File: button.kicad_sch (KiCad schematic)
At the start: 4 parts

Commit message: started to work on power part
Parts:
- SW1: renamed from SW?; footprint (none) -> Button_Switch_SMD:SW_Push_1P1T_NO_6x6mm_H9.5mm
- gave numbers to parts that had none: 3
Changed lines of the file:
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@@
   (symbol (lib_id "power:GND") (at 108.585 89.535 0) (unit 1)
     (in_bom yes) (on_board yes) (fields_autoplaced)
-    (property "Reference" "#PWR?" (id 0) (at 108.585 95.885 0)
+    (property "Reference" "#PWR030" (id 0) (at 108.585 95.885 0)
       (effects (font (size 1.27 1.27)) hide)
     )
@@
   (symbol (lib_id "Switch:SW_Push") (at 108.585 82.55 270) (unit 1)
     (in_bom yes) (on_board yes) (fields_autoplaced)
-    (property "Reference" "SW?" (id 0) (at 113.03 81.2799 90)
+    (property "Reference" "SW1" (id 0) (at 113.03 81.2799 90)
       (effects (font (size 1.27 1.27)) (justify left))
     )
@@
       (effects (font (size 1.27 1.27)) (justify left))
     )
-    (property "Footprint" "" (id 2) (at 113.665 82.55 0)
+    (property "Footprint" "Button_Switch_SMD:SW_Push_1P1T_NO_6x6mm_H9.5mm" (id 2) (at 113.665 82.55 0)
       (effects (font (size 1.27 1.27)) hide)
     )
@@
   (symbol (lib_id "eurorack:R-10k-1206") (at 108.585 71.755 0) (unit 1)
     (in_bom yes) (on_board yes) (fields_autoplaced)
-    (property "Reference" "R?" (id 0) (at 110.49 70.4849 0)
+    (property "Reference" "R28" (id 0) (at 110.49 70.4849 0)
       (effects (font (size 1.27 1.27)) (justify left))
     )
@@
   (symbol (lib_id "eurorack:C-100nF-0805") (at 96.52 83.185 0) (unit 1)
     (in_bom yes) (on_board yes)
-    (property "Reference" "C?" (id 0) (at 97.79 85.725 0)
+    (property "Reference" "C9" (id 0) (at 97.79 85.725 0)
       (effects (font (size 1.27 1.27)) (justify left))
     )
@@
   (symbol (lib_id "power:+3V3") (at 108.585 66.04 0) (unit 1)
     (in_bom yes) (on_board yes) (fields_autoplaced)
-    (property "Reference" "#PWR?" (id 0) (at 108.585 69.85 0)
+    (property "Reference" "#PWR029" (id 0) (at 108.585 69.85 0)
       (effects (font (size 1.27 1.27)) hide)
     )
@@
   (symbol (lib_id "eurorack:R-100-1206") (at 102.87 77.47 270) (unit 1)
     (in_bom yes) (on_board yes)
-    (property "Reference" "R?" (id 0) (at 101.6 80.01 90))
+    (property "Reference" "R27" (id 0) (at 101.6 80.01 90))
     (property "Value" "R-100-1206" (id 1) (at 99.06 74.93 90))
     (property "Footprint" "Resistor_SMD:R_1206_3216Metric_Pad1.30x1.75mm_HandSolder" (id 2) (at 102.87 75.692 90)

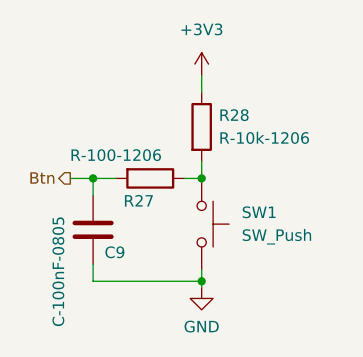
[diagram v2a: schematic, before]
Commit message: refactoring with global labels
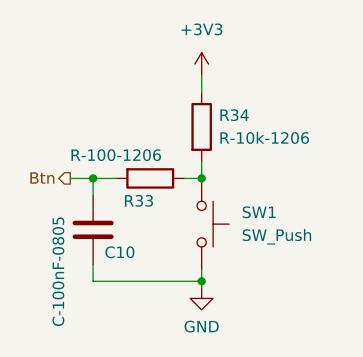
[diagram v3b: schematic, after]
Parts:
- renumbered C9 to C10, R27 to R33, R28 to R34
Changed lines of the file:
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@@
   (symbol (lib_id "power:GND") (at 108.585 89.535 0) (unit 1)
     (in_bom yes) (on_board yes) (fields_autoplaced)
-    (property "Reference" "#PWR030" (id 0) (at 108.585 95.885 0)
+    (property "Reference" "#PWR036" (id 0) (at 108.585 95.885 0)
       (effects (font (size 1.27 1.27)) hide)
     )
@@
   (symbol (lib_id "eurorack:R-10k-1206") (at 108.585 71.755 0) (unit 1)
     (in_bom yes) (on_board yes) (fields_autoplaced)
-    (property "Reference" "R28" (id 0) (at 110.49 70.4849 0)
+    (property "Reference" "R34" (id 0) (at 110.49 70.4849 0)
       (effects (font (size 1.27 1.27)) (justify left))
     )
@@
   (symbol (lib_id "eurorack:C-100nF-0805") (at 96.52 83.185 0) (unit 1)
     (in_bom yes) (on_board yes)
-    (property "Reference" "C9" (id 0) (at 97.79 85.725 0)
+    (property "Reference" "C10" (id 0) (at 97.79 85.725 0)
       (effects (font (size 1.27 1.27)) (justify left))
     )
@@
   (symbol (lib_id "power:+3V3") (at 108.585 66.04 0) (unit 1)
     (in_bom yes) (on_board yes) (fields_autoplaced)
-    (property "Reference" "#PWR029" (id 0) (at 108.585 69.85 0)
+    (property "Reference" "#PWR035" (id 0) (at 108.585 69.85 0)
       (effects (font (size 1.27 1.27)) hide)
     )
@@
   (symbol (lib_id "eurorack:R-100-1206") (at 102.87 77.47 270) (unit 1)
     (in_bom yes) (on_board yes)
-    (property "Reference" "R27" (id 0) (at 101.6 80.01 90))
+    (property "Reference" "R33" (id 0) (at 101.6 80.01 90))
     (property "Value" "R-100-1206" (id 1) (at 99.06 74.93 90))
     (property "Footprint" "Resistor_SMD:R_1206_3216Metric_Pad1.30x1.75mm_HandSolder" (id 2) (at 102.87 75.692 90)

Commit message: cleaning into modules
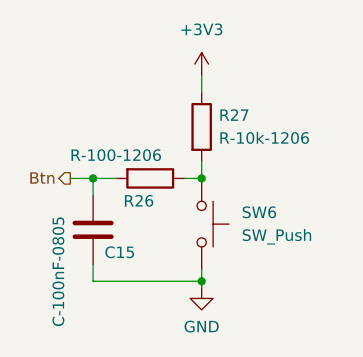
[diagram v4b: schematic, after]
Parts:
- renumbered C10 to C15, R33 to R26, R34 to R27, SW1 to SW6
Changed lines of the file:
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@@
     (effects (font (size 1.27 1.27)) (justify right))
   )
-  (symbol (lib_id "power:GND") (at 108.585 89.535 0) (unit 1)
+  (symbol (lib_id "power:GND") (at 108.585 89.535 0)
     (in_bom yes) (on_board yes) (fields_autoplaced)
-    (property "Reference" "#PWR036" (id 0) (at 108.585 95.885 0)
+    (property "Reference" "#PWR061" (id 0) (at 108.585 95.885 0)
       (effects (font (size 1.27 1.27)) hide)
     )
@@
     (pin "1")
   )
-  (symbol (lib_id "Switch:SW_Push") (at 108.585 82.55 270) (unit 1)
+  (symbol (lib_id "Switch:SW_Push") (at 108.585 82.55 270)
     (in_bom yes) (on_board yes) (fields_autoplaced)
-    (property "Reference" "SW1" (id 0) (at 113.03 81.2799 90)
+    (property "Reference" "SW6" (id 0) (at 113.03 81.2799 90)
       (effects (font (size 1.27 1.27)) (justify left))
     )
@@
     (pin "2")
   )
-  (symbol (lib_id "eurorack:R-10k-1206") (at 108.585 71.755 0) (unit 1)
+  (symbol (lib_id "eurorack:R-10k-1206") (at 108.585 71.755 0)
     (in_bom yes) (on_board yes) (fields_autoplaced)
-    (property "Reference" "R34" (id 0) (at 110.49 70.4849 0)
+    (property "Reference" "R27" (id 0) (at 110.49 70.4849 0)
       (effects (font (size 1.27 1.27)) (justify left))
     )
@@
     (pin "2")
   )
-  (symbol (lib_id "eurorack:C-100nF-0805") (at 96.52 83.185 0) (unit 1)
+  (symbol (lib_id "eurorack:C-100nF-0805") (at 96.52 83.185 0)
     (in_bom yes) (on_board yes)
-    (property "Reference" "C10" (id 0) (at 97.79 85.725 0)
+    (property "Reference" "C15" (id 0) (at 97.79 85.725 0)
       (effects (font (size 1.27 1.27)) (justify left))
     )
@@
     (pin "2")
   )
-  (symbol (lib_id "power:+3V3") (at 108.585 66.04 0) (unit 1)
+  (symbol (lib_id "power:+3V3") (at 108.585 66.04 0)
     (in_bom yes) (on_board yes) (fields_autoplaced)
-    (property "Reference" "#PWR035" (id 0) (at 108.585 69.85 0)
+    (property "Reference" "#PWR060" (id 0) (at 108.585 69.85 0)
       (effects (font (size 1.27 1.27)) hide)
     )
@@
     (pin "1")
   )
-  (symbol (lib_id "eurorack:R-100-1206") (at 102.87 77.47 270) (unit 1)
+  (symbol (lib_id "eurorack:R-100-1206") (at 102.87 77.47 270)
     (in_bom yes) (on_board yes)
-    (property "Reference" "R33" (id 0) (at 101.6 80.01 90))
+    (property "Reference" "R26" (id 0) (at 101.6 80.01 90))
     (property "Value" "R-100-1206" (id 1) (at 99.06 74.93 90))
     (property "Footprint" "Resistor_SMD:R_1206_3216Metric_Pad1.30x1.75mm_HandSolder" (id 2) (at 102.87 75.692 90)

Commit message: working on AD inputs
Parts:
- renumbered R26 to R40, R27 to R41
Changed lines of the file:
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@@
   (symbol (lib_id "power:GND") (at 108.585 89.535 0)
     (in_bom yes) (on_board yes) (fields_autoplaced)
-    (property "Reference" "#PWR062" (id 0) (at 108.585 95.885 0)
+    (property "Reference" "#PWR097" (id 0) (at 108.585 95.885 0)
       (effects (font (size 1.27 1.27)) hide)
     )
@@
   (symbol (lib_id "eurorack:R-10k-1206") (at 108.585 71.755 0)
     (in_bom yes) (on_board yes) (fields_autoplaced)
-    (property "Reference" "R27" (id 0) (at 110.49 70.4849 0)
+    (property "Reference" "R41" (id 0) (at 110.49 70.4849 0)
       (effects (font (size 1.27 1.27)) (justify left))
     )
@@
   (symbol (lib_id "power:+3V3") (at 108.585 66.04 0)
     (in_bom yes) (on_board yes) (fields_autoplaced)
-    (property "Reference" "#PWR061" (id 0) (at 108.585 69.85 0)
+    (property "Reference" "#PWR096" (id 0) (at 108.585 69.85 0)
       (effects (font (size 1.27 1.27)) hide)
     )
@@
   (symbol (lib_id "eurorack:R-100-1206") (at 102.87 77.47 270)
     (in_bom yes) (on_board yes)
-    (property "Reference" "R26" (id 0) (at 101.6 80.01 90))
+    (property "Reference" "R40" (id 0) (at 101.6 80.01 90))
     (property "Value" "R-100-1206" (id 1) (at 99.06 74.93 90))
     (property "Footprint" "Resistor_SMD:R_1206_3216Metric_Pad1.30x1.75mm_HandSolder" (id 2) (at 102.87 75.692 90)

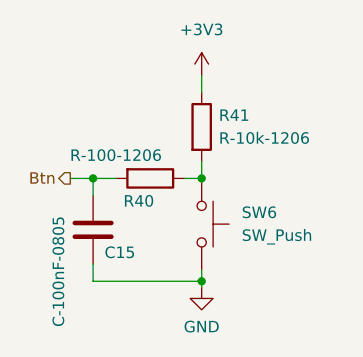
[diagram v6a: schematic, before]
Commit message: reannotated changed to LM324
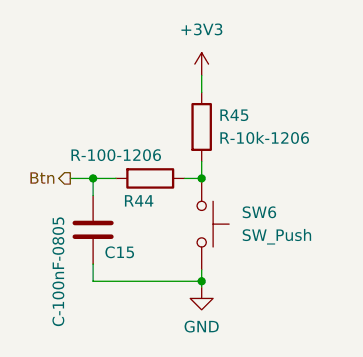
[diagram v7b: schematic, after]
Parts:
- renumbered R40 to R44, R41 to R45
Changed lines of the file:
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@@
   (symbol (lib_id "power:GND") (at 108.585 89.535 0)
     (in_bom yes) (on_board yes) (fields_autoplaced)
-    (property "Reference" "#PWR097" (id 0) (at 108.585 95.885 0)
+    (property "Reference" "#PWR069" (id 0) (at 108.585 95.885 0)
       (effects (font (size 1.27 1.27)) hide)
     )
@@
   (symbol (lib_id "eurorack:R-10k-1206") (at 108.585 71.755 0)
     (in_bom yes) (on_board yes) (fields_autoplaced)
-    (property "Reference" "R41" (id 0) (at 110.49 70.4849 0)
+    (property "Reference" "R45" (id 0) (at 110.49 70.4849 0)
       (effects (font (size 1.27 1.27)) (justify left))
     )
@@
   (symbol (lib_id "power:+3V3") (at 108.585 66.04 0)
     (in_bom yes) (on_board yes) (fields_autoplaced)
-    (property "Reference" "#PWR096" (id 0) (at 108.585 69.85 0)
+    (property "Reference" "#PWR068" (id 0) (at 108.585 69.85 0)
       (effects (font (size 1.27 1.27)) hide)
     )
@@
   (symbol (lib_id "eurorack:R-100-1206") (at 102.87 77.47 270)
     (in_bom yes) (on_board yes)
-    (property "Reference" "R40" (id 0) (at 101.6 80.01 90))
+    (property "Reference" "R44" (id 0) (at 101.6 80.01 90))
     (property "Value" "R-100-1206" (id 1) (at 99.06 74.93 90))
     (property "Footprint" "Resistor_SMD:R_1206_3216Metric_Pad1.30x1.75mm_HandSolder" (id 2) (at 102.87 75.692 90)

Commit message: Made the first proposed layout
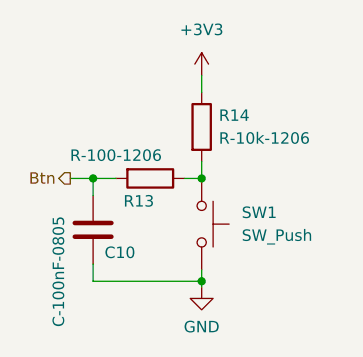
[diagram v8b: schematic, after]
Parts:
- SW1: renamed from SW6; footprint Button_Switch_SMD:SW_Push_1P1T_NO_6x6mm_H9.5mm -> Button_Switch_THT:SW_PUSH_6mm_H9.5mm
- renumbered C15 to C10, R44 to R13, R45 to R14
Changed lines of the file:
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@@
   (symbol (lib_id "power:GND") (at 108.585 89.535 0)
     (in_bom yes) (on_board yes) (fields_autoplaced)
-    (property "Reference" "#PWR069" (id 0) (at 108.585 95.885 0)
+    (property "Reference" "#PWR031" (id 0) (at 108.585 95.885 0)
       (effects (font (size 1.27 1.27)) hide)
     )
@@
   (symbol (lib_id "Switch:SW_Push") (at 108.585 82.55 270)
     (in_bom yes) (on_board yes) (fields_autoplaced)
-    (property "Reference" "SW6" (id 0) (at 113.03 81.2799 90)
+    (property "Reference" "SW1" (id 0) (at 113.03 81.2799 90)
       (effects (font (size 1.27 1.27)) (justify left))
     )
@@
       (effects (font (size 1.27 1.27)) (justify left))
     )
-    (property "Footprint" "Button_Switch_SMD:SW_Push_1P1T_NO_6x6mm_H9.5mm" (id 2) (at 113.665 82.55 0)
+    (property "Footprint" "Button_Switch_THT:SW_PUSH_6mm_H9.5mm" (id 2) (at 113.665 82.55 0)
       (effects (font (size 1.27 1.27)) hide)
     )
@@
   (symbol (lib_id "eurorack:R-10k-1206") (at 108.585 71.755 0)
     (in_bom yes) (on_board yes) (fields_autoplaced)
-    (property "Reference" "R45" (id 0) (at 110.49 70.4849 0)
+    (property "Reference" "R14" (id 0) (at 110.49 70.4849 0)
       (effects (font (size 1.27 1.27)) (justify left))
     )
@@
   (symbol (lib_id "eurorack:C-100nF-0805") (at 96.52 83.185 0)
     (in_bom yes) (on_board yes)
-    (property "Reference" "C15" (id 0) (at 97.79 85.725 0)
+    (property "Reference" "C10" (id 0) (at 97.79 85.725 0)
       (effects (font (size 1.27 1.27)) (justify left))
     )
@@
   (symbol (lib_id "power:+3V3") (at 108.585 66.04 0)
     (in_bom yes) (on_board yes) (fields_autoplaced)
-    (property "Reference" "#PWR068" (id 0) (at 108.585 69.85 0)
+    (property "Reference" "#PWR030" (id 0) (at 108.585 69.85 0)
       (effects (font (size 1.27 1.27)) hide)
     )
@@
   (symbol (lib_id "eurorack:R-100-1206") (at 102.87 77.47 270)
     (in_bom yes) (on_board yes)
-    (property "Reference" "R44" (id 0) (at 101.6 80.01 90))
+    (property "Reference" "R13" (id 0) (at 101.6 80.01 90))
     (property "Value" "R-100-1206" (id 1) (at 99.06 74.93 90))
     (property "Footprint" "Resistor_SMD:R_1206_3216Metric_Pad1.30x1.75mm_HandSolder" (id 2) (at 102.87 75.692 90)
